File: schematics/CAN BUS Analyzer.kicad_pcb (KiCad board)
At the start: 2 copper layers, 5 parts, among them J1 DE9_Pins_MountingHoles, J2 Conn_01x04, J3 Conn_01x06, U1 ATSAME51J18A-A, U2 TCAN1043xDxQ1

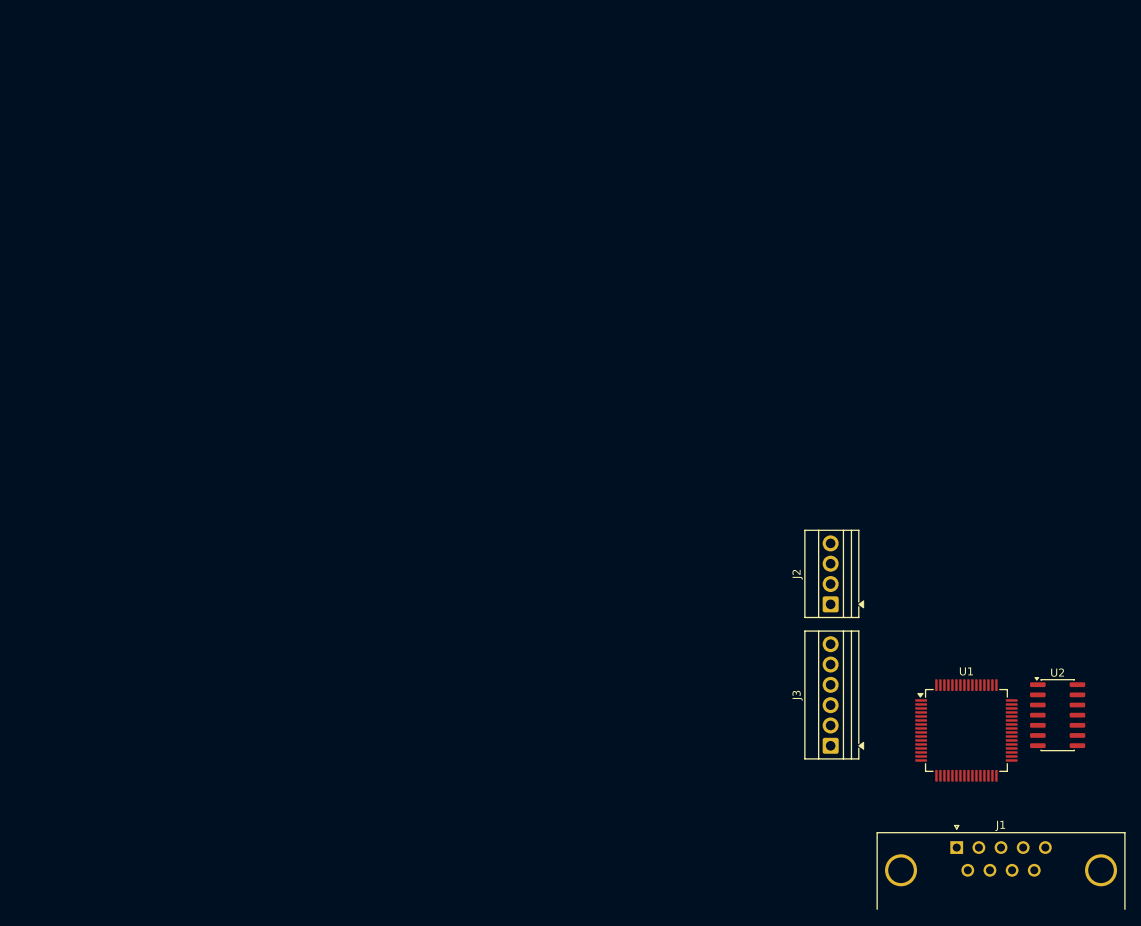
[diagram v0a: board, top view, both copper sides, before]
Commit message: update pcb size and shape
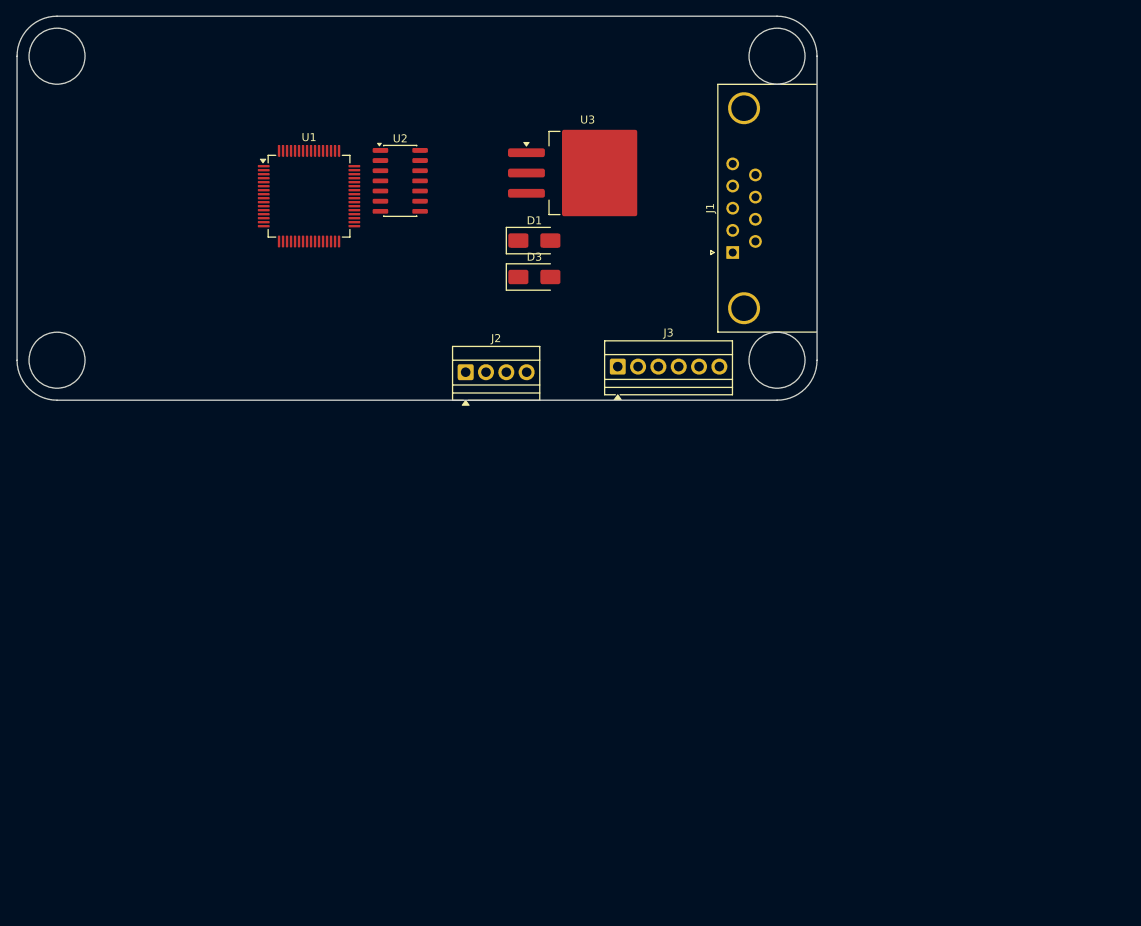
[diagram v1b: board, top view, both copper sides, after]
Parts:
- added D1: US1G, Diode_SMD:D_SMA, F.Cu at (64.7, 28.1)
- added D3: US1G, Diode_SMD:D_SMA, F.Cu at (64.7, 32.6)
- added U3: LM2937xS, Package_TO_SOT_SMD:TO-263-3_TabPin2, F.Cu at (71.3, 19.6)
- J1: footprint Connector_Dsub:DSUB-9_Pins_Horizontal_P2.77x2.84mm_EdgePinOffset4.94mm_Housed_MountingHolesOffset4.94mm -> Connector_Dsub:DSUB-9_Pins_Horizontal_P2.77x2.84mm_EdgePinOffset7.70mm_Housed_MountingHolesOffset9.12mm
- moved U1 105.9 mm to (36.5, 22.5)
- moved U2 105.9 mm to (47.9, 20.6)
- moved J1 79.5 mm to (89.5, 29.5), turned to 90 degrees
- moved J3 54.4 mm to (75.1, 43.8), turned to 0 degrees
- moved J2 54.1 mm to (56.1, 44.5), turned to 0 degrees
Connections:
- J1 pad 2: unconnected-(J1-Pad2) -> CAN_1_LOW
- J1 pad 3: unconnected-(J1-Pad3) -> GND
- J1 pad 6: unconnected-(J1-Pad6) -> GND
- J1 pad 7: unconnected-(J1-Pad7) -> CAN_1_HIGH
- J2 pad 1: unconnected-(J2-Pin_1-Pad1) -> IOVL2
- J2 pad 2: unconnected-(J2-Pin_2-Pad2) -> GND
- J2 pad 3: unconnected-(J2-Pin_3-Pad3) -> GND
- J2 pad 4: unconnected-(J2-Pin_4-Pad4) -> IOVL1
- J3 pad 1: unconnected-(J3-Pin_1-Pad1) -> VCC
- J3 pad 6: unconnected-(J3-Pin_6-Pad6) -> GND
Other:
- board outline added: 100 x 48 mm

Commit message: smaller changes, cpu and conn
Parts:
- added J5: USB_B, Connector_USB:USB_B_OST_USB-B1HSxx_Horizontal, F.Cu at (15.1, 20.6)
- added J6: Conn_ARM_JTAG_SWD_10, Connector_PinHeader_1.27mm:PinHeader_2x05_P1.27mm_Vertical, F.Cu at (64.1, 20.9)
- moved D1 42.5 mm to (23.9, 40.0)
- moved D3 42.5 mm to (23.9, 44.6)
- moved U3 42.5 mm to (30.6, 31.6)
- moved U2 28.6 mm to (74.4, 9.71)
- moved U1 28.0 mm to (61.4, 9.72), turned to 180 degrees
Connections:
- U1 pad 45: unconnected-(U1-PA24-Pad45) -> USB D-
- U1 pad 46: unconnected-(U1-PA25-Pad46) -> USB D+
- U1 pad 52: unconnected-(U1-~{RESET}-Pad52) -> Net-(U1-~{RESET})
- U1 pad 57: unconnected-(U1-PA30-Pad57) -> SWCLK
- U1 pad 58: unconnected-(U1-PA31-Pad58) -> SWDIO
